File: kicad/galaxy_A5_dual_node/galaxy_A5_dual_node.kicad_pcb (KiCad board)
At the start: 2 copper layers, 60 x 80 mm, 88 parts, among them J1 Conn, J2 Conn, J3 USB_C_Receptacle_PowerOnly_6P, J4 Conn_01x02_Socket, J5 Conn_01x02_Socket, Q1 DTC143Z, Q2 DTC143Z, Q3 DTC143Z, Q4 DTC143Z, SW1 SW_MAIN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

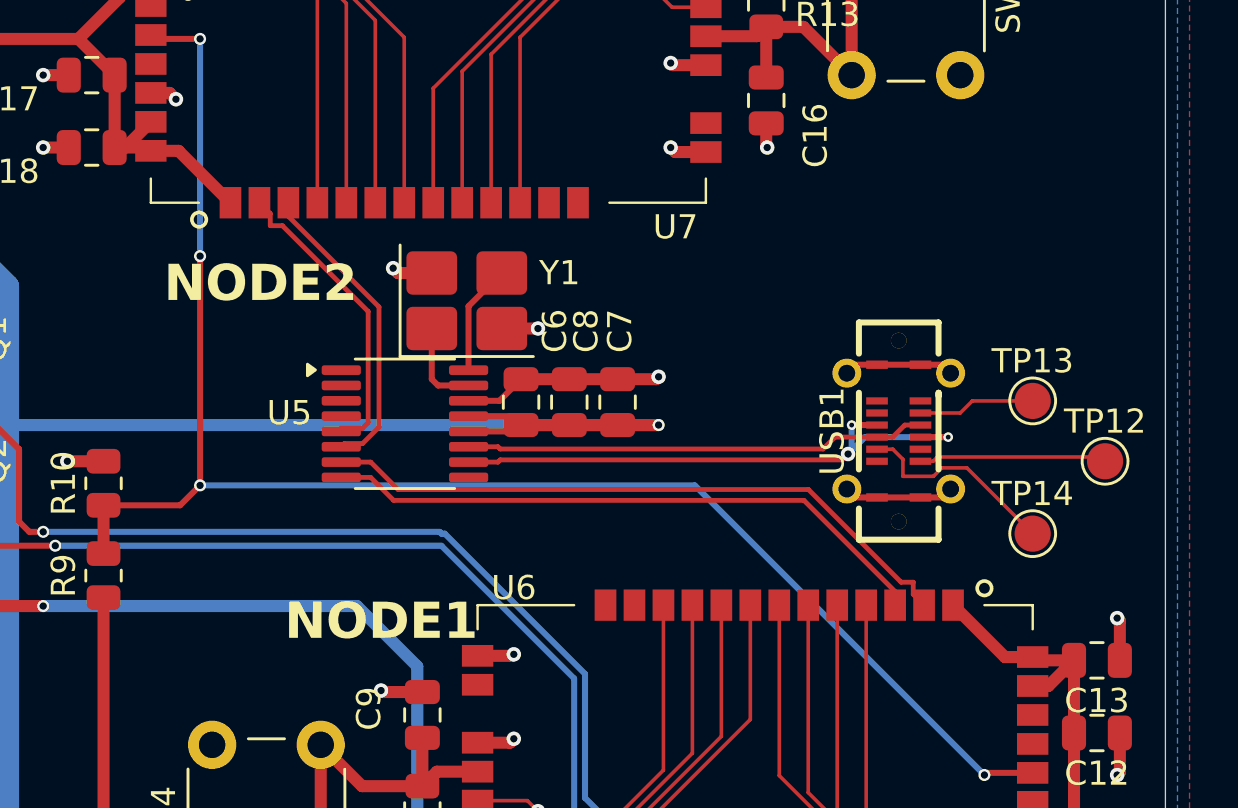
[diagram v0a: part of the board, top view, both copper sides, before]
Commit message: fixed USB CC, VBUS RAK
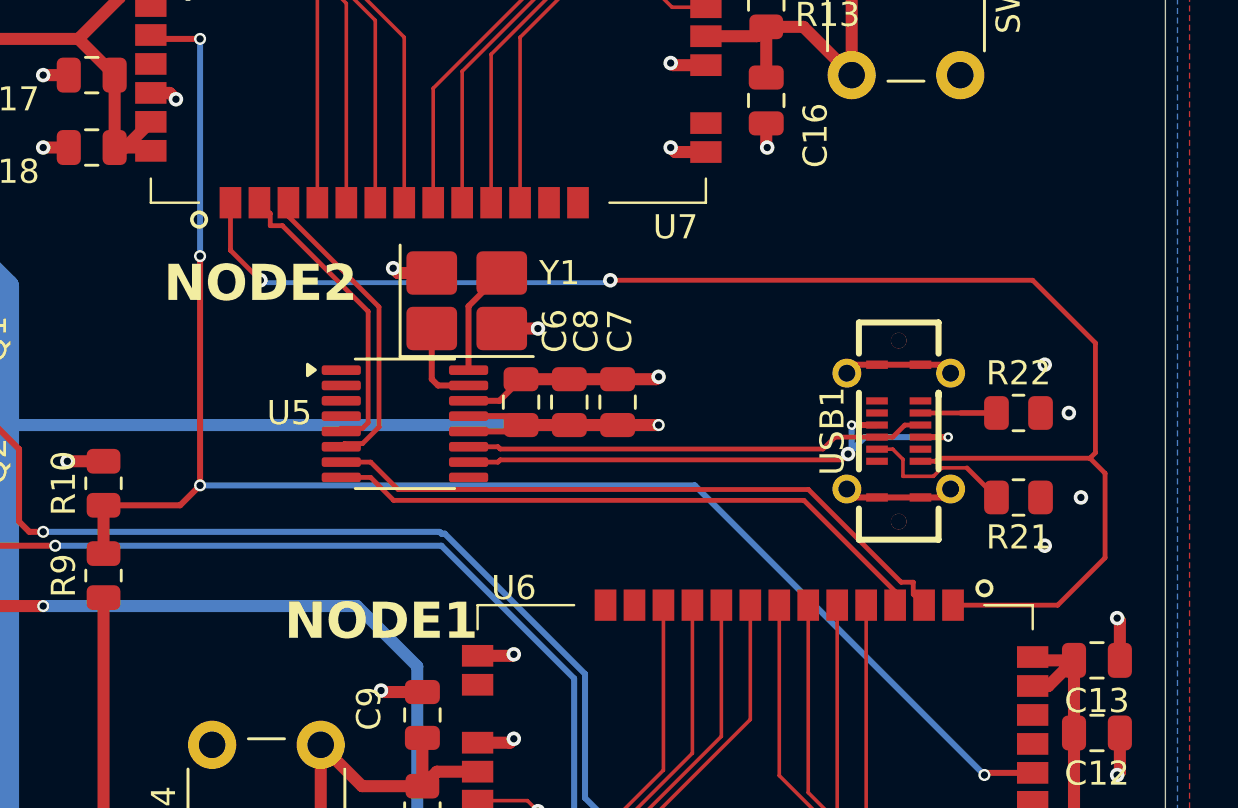
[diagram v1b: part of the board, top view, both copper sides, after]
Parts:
- removed TP12: VBUS, TestPoint:TestPoint_Pad_D1.5mm
- removed TP13: CC2, TestPoint:TestPoint_Pad_D1.5mm
- removed TP14: CC1, TestPoint:TestPoint_Pad_D1.5mm
- added R21: 5.1k, Resistor_SMD:R_0805_2012Metric, F.Cu at (173.9, 94.5)
- added R22: 5.1k, Resistor_SMD:R_0805_2012Metric, F.Cu at (173.9, 91.0)
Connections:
- U6 pad 1: VDD_RAK1 -> VBUS
- U7 pad 1: VDD_RAK2 -> VBUS
- USB1 pad B9: Net-(TP12-Pad1) -> VBUS
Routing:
- net VBUS: track 0.00 -> 62.9 mm, vias 0 -> 2
- net Net-(TP12-Pad1): track 7.80 -> 0.00 mm
- net VDD_RAK1: track 119.3 -> 115.2 mm
- net VDD_RAK2: track 94.8 -> 90.6 mm
- net Net-(USB1-CC1): track 8.60 -> 6.48 mm
- net Net-(USB1-CC2): track 4.86 -> 6.30 mm
- net GND: vias 43 -> 47

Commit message: update pcb version number
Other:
- board text added: "Meshtastic Galaxy A5 Dual Node Main PCB V1.1 03.05.2026 by DerRKDCB"
- board text removed: "Meshtastic Galaxy A5 Dual Node Main PCB V1.0 22.02.2026 by DerRKDCB"
